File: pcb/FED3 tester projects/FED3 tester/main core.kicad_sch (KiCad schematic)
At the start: 39 parts, among them J6 Conn_02x03_Odd_Even, Q2 DMN63D8L-7, SW1 SW_SPST, SW2 SW_SPST, SW3 SW_SPST, SW4 SW_SPST, SW5 SW_SPST, U9 ATXMEGA32A4U-MH

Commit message: FED3 Tester - 1º routing finalizado
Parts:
- removed C36: 100nF, Capacitor_SMD:C_0402_1005Metric_Pad0.74x0.62mm_HandSolder, symbol Device:C_Small
- C26, C27, C28, C29, C30, C31, C32, C33, C34, C35: footprint Capacitor_SMD:C_0402_1005Metric_Pad0.74x0.62mm_HandSolder -> Capacitor_SMD:C_0402_1005Metric

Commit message: FED3-tester
- 'final' - antes de revisão com o Filipe
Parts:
- removed R31, R32, R33, R34, R35: 100R, Resistor_SMD:R_0402_1005Metric, symbol Device:R_US
- BZ1: MPN (none) -> CSS-0575A-SMT-TR; OEPSPN (none) -> TBD; TYPE (none) -> SMD
- C26, C27, C28, C29, C30, C31, C32, C33, C34, C35: MPN C1005X7R1E104K050BB -> CGA2B3X7R1H104K050BB; OEPSPN OEPS010050 -> OEPS010016; TYPE (none) -> SMD
- D2, D7, OSC1, Q2, R36, R38, R39, R40, R41, R42, SW1, SW2, SW3, SW4, SW5, U9: TYPE (none) -> SMD
- D3, D4, D5, D6: OEPSPN OEPS030005 -> OEPS030005; TYPE (none) -> SMD
- J6: TYPE (none) -> TH
- R37: MPN OEPS020043 -> CPF0402B10KE1; OEPSPN CPF0402B10KE1 -> OEPS020043; TYPE (none) -> SMD
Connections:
- net Buzzer_NOK: now also SW3.2
- net Buzzer_OK: now also SW2.2
- net Motor_NOK: now also SW5.2
- net Motor_OK: now also SW4.2
- net START_SW: now also SW1.2
- no-connect marks 5 -> 6
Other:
- moved on the sheet: C26, C31, C32, C33, C34

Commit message: FED 3 tester - actualizados novos OEPSPN & MPN; ainda 1 em falta
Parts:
- BZ1: OEPSPN TBD -> OEPS100079
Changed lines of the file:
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@@
 			)
 		)
-		(property "OEPSPN" "TBD"
+		(property "OEPSPN" "OEPS100079"
 			(at 261.62 143.51 0)
 			(effects

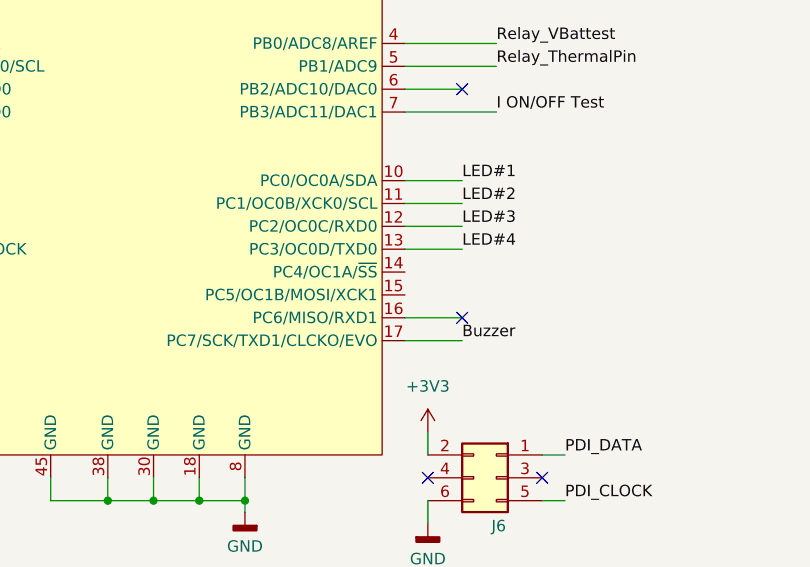
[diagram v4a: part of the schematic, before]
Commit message: tunning com v.7.7
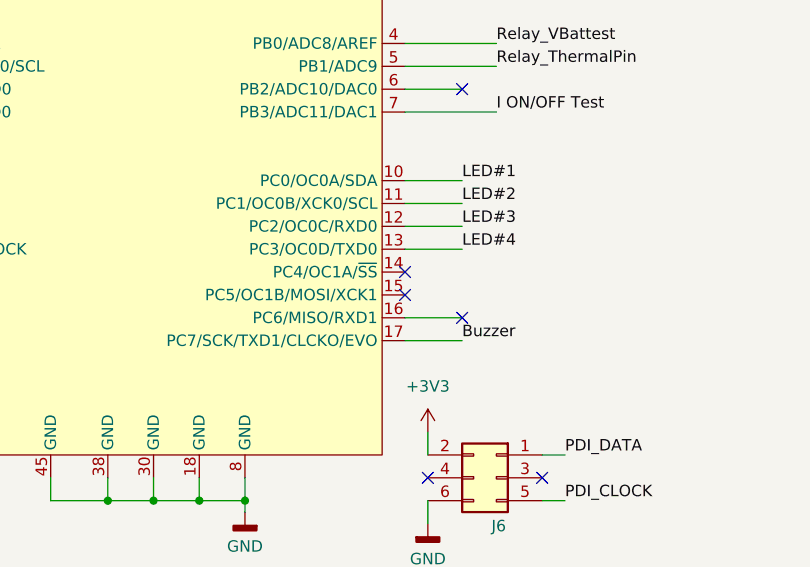
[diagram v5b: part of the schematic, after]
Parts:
- BZ1: TYPE SMD -> (none); Voltage (none) -> 3V
- C26, C27, C28, C29, C30, C31, C32, C33, C34, C35: TYPE SMD -> (none); TempCo (none) -> X7R; Tolerance (none) -> 10%; Voltage (none) -> 50V
- D2, D3, D4, D5, D6, D7, OSC1, Q2, SW1, SW2, SW3, SW4, SW5, U9: TYPE SMD -> (none)
- J6: TYPE TH -> (none)
- R36, R38, R39, R40, R41, R42: TYPE SMD -> (none); Tolerance (none) -> 1%
- R37: TYPE SMD -> (none); Tolerance (none) -> 0.1%
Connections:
- no-connect marks 6 -> 8

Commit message: FED3 tester project
.commit para sincronia
.ainda longe do final
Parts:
- removed C27: 100nF, Capacitor_SMD:C_0402_1005Metric, symbol Device:C_Small
- added C22, C23, C24, C25: 100nF, Capacitor_SMD:C_0402_1005Metric, symbol Device:C_Small
- added D5, D8: Green, LED_SMD:LED_0603_1608Metric, symbol Device:LED
- added D9: Red, LED_SMD:LED_0603_1608Metric, symbol Device:LED
- added R13, R17: 2k, Resistor_SMD:R_0402_1005Metric, symbol Device:R_US
- added R18: 10k, Resistor_SMD:R_0402_1005Metric, symbol Device:R_US
- added SW2, SW3, SW4, SW5: SW_SPST, Button_Switch_SMD:SW_SPST_TL3305B, symbol Switch:SW_Push
- D1: renamed from D7; value Green LED -> Green
- D2: renamed from D6; value Green LED -> Green
- D3: renamed from D5; value Green LED -> Green
- D4: value Green LED -> Green
- D7: renamed from D3; value Green LED -> Red; MPN LTST-C191KGKT -> VFHR1116P-4C82A-TR; OEPSPN OEPS030005 -> OEPS030038
- R10: renamed from R41; value 330R -> 2k; MPN CRCW0402330RFKEDHP -> ERJ-2RKF2001X; OEPSPN OEPS020191 -> OEPS020007
- R11: renamed from R40; value 330R -> 2k; MPN CRCW0402330RFKEDHP -> ERJ-2RKF2001X; OEPSPN OEPS020191 -> OEPS020007
- R12: renamed from R39; value 330R -> 2k; MPN CRCW0402330RFKEDHP -> ERJ-2RKF2001X; OEPSPN OEPS020191 -> OEPS020007
- R15: renamed from R38; value 330R -> 10k; MPN CRCW0402330RFKEDHP -> ERJ-2RKF1002X; OEPSPN OEPS020191 -> OEPS020013
- R9: renamed from R42; value 560R -> 2k; MPN CRCW0402560RFKED -> ERJ-2RKF2001X; OEPSPN OEPS020193 -> OEPS020007
- renumbered C26 to C18, C28 to C19, C29 to C20, C30 to C21, C35 to C26, C33 to C27, C34 to C28, C31 to C29, C32 to C30, D2 to D6, J6 to J2, Q2 to Q1, R36 to R14, R37 to R16, SW4 to SW6, SW5 to SW7, SW2 to SW8, SW3 to SW9, U9 to U5
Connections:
- net VUSB_check is gone; now on net VBattest_check: U5.41 (PA1/ADC1)
- net ~{RESET}_Test is gone; now on net Motor_NOK: U5.26 (PD6/RXD1/MISO/D-)
- net +3V3: no longer U5.39 (AVCC)
- net Buzzer_NOK: now also U5.40 (PA0/ADC0/AREF); no longer U5.22 (PD2/OC0C/RXD0)
- net Buzzer_OK: now also U5.27 (PD7/TXD1/SCK/CLCKO/D+); no longer U5.21 (PD1/OC0B/XCK0)
- net GND: now also C22.2, C23.2, C24.2, C25.2, D5.1 (K), D8.1 (K), D9.1 (K), SW2.1, SW3.1, SW4.1, SW5.1
- net I ON/OFF Test: now also U5.6 (PB2/ADC10/DAC0); no longer U5.7 (PB3/ADC11/DAC1)
- net LED#1: now also R9.2; no longer R12.2
- net LED#2: now also R10.2; no longer R11.2
- net LED#3: now also R11.2; no longer R10.2
- net LED#4: now also R12.2; no longer R9.2
- net Motor_NOK: no longer U5.24 (PD4/OC1A/~{SS})
- net Motor_OK: now also U5.25 (PD5/OC1B/XCK1/MOSI); no longer U5.23 (PD3/OC0D/TXD0)
- net POWER_EN: now also U5.7 (PB3/ADC11/DAC1); no longer U5.27 (PD7/TXD1/SCK/CLCKO/D+)
- net VBattest_check: no longer U5.40 (PA0/ADC0/AREF)
- net VccRGB_check: no longer U5.42 (PA2/ADC2)
- net LED#5: now reaches U5.14 (PC4/OC1A/~{SS})
- net LED#5: now also R13.2
- net PASS: now reaches U5.15 (PC5/OC1B/MOSI/XCK1)
- net PASS: now also R17.2
- net FAIL: now reaches U5.16 (PC6/MISO/RXD1)
- net FAIL: now also R18.2
- new net: D8.2 (A), R17.1
- new net: D9.2 (A), R18.1
- new net: D5.2 (A), R13.1
- new net AVCC: U5.39 (AVCC)
- new net Prog_NOK: C23.1, SW3.2, U5.22 (PD2/OC0C/RXD0)
- new net Prog_OK: C22.1, SW2.2, U5.21 (PD1/OC0B/XCK0)
- new net RGBW_NOK: C25.1, SW5.2, U5.24 (PD4/OC1A/~{SS})
- new net RGBW_OK: C24.1, SW4.2, U5.23 (PD3/OC0D/TXD0)
- new net VUSB_2DUT: U5.42 (PA2/ADC2)
- no-connect marks 8 -> 3
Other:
- sheet DUT stage ports: added VUSB_2DUT; removed VUSB_check, ~{RESET}_Test
- moved on the sheet: C18, C19, C20, C21, C26, C27, C28, C29, C30, D1, D2, D3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

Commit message: FED3 tester - sync of the week
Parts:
- renumbered C18 to C17, C19 to C18, C20 to C19, C21 to C20, C22 to C21, C23 to C22, C24 to C23, C25 to C24, C26 to C25, C27 to C26, C28 to C27, C29 to C28, C30 to C29

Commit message: FED3 tester rev.B & FED3 tester support rev.B
-rev.B para 1ª revisão do Filipe
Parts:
- removed D2: Green, LED_SMD:LED_0603_1608Metric, symbol Device:LED
- removed R10: 2k, Resistor_SMD:R_0402_1005Metric, symbol Device:R_US
- renumbered C17 to C16, C18 to C17, C19 to C18, C20 to C19, C21 to C20, C22 to C21, C23 to C22, C24 to C23, C25 to C24, C26 to C25, C27 to C26, C28 to C27, C29 to C28, D3 to D2, D4 to D3, D5 to D4, D6 to D5, D7 to D6, D8 to D7, D9 to D8, R11 to R10, R12 to R11, R13 to R12, R14 to R13, R15 to R14, R16 to R15, R17 to R16, R18 to R17
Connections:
- net LED#2: now also R10.2
- net LED#3: now also R11.2; no longer R10.2
- net LED#4: now also R12.2; no longer R11.2
- net VUSB_2DUT: now also U5.14 (PC4/OC1A/~{SS}); no longer U5.42 (PA2/ADC2)
- net VccRGB_check: now also U5.42 (PA2/ADC2)
- net I ON/OFF Test renamed I_ON/OFF_Test
- removed net LED#5: R12.2, U5.14 (PC4/OC1A/~{SS})
